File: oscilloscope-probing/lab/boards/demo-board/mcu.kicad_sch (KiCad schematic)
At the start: 75 parts, among them J4 CORTEX_DEBUG_ETM, J6 CONN_01X06, SW3 SWITCH, SW4 SWITCH, SW5 SWITCH, SW6 SWITCH, SW7 SWITCH, U4 XC7A35T-2FGG484I, U5 STM32H750XBH6, U6 ECS-1612MV-250-CN, U7 ECS-1612MV-250-CN, U8 S25FL064LABMFI013

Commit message: Continued routing demo board
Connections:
- net DPAD_N: now also U5.N15 (PJ6); no longer U5.E10 (PJ13)
- net DPAD_S: now also U5.L14 (PJ10); no longer U5.D11 (PJ12)
- net DPAD_SEL: now also U5.M14 (PJ9); no longer U5.D10 (PJ14)
- net DPAD_W: now also U5.N14 (PJ7); no longer U5.L14 (PJ10)
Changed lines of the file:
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@@
 	)
 	(no_connect
-		(at 107.95 232.41)
-	)
-	(no_connect
 		(at 35.56 140.97)
 	)
@@
 	)
 	(no_connect
+		(at 107.95 247.65)
+	)
+	(no_connect
 		(at 107.95 222.25)
 	)
@@
 	)
 	(no_connect
+		(at 107.95 250.19)
+	)
+	(no_connect
 		(at 107.95 148.59)
 	)
@@
 	)
 	(no_connect
-		(at 107.95 240.03)
-	)
-	(no_connect
 		(at 35.56 101.6)
 	)
@@
 	)
 	(no_connect
-		(at 107.95 234.95)
+		(at 107.95 57.15)
 	)
 	(no_connect
-		(at 107.95 57.15)
+		(at 107.95 252.73)
 	)
 	(no_connect
@@
 	)
 	(label "DPAD_S"
-		(at 107.95 247.65 180)
+		(at 107.95 242.57 180)
 		(effects
 			(font
@@
 	)
 	(label "DPAD_W"
-		(at 107.95 242.57 180)
+		(at 107.95 234.95 180)
 		(effects
 			(font
@@
 	)
 	(label "DPAD_SEL"
-		(at 107.95 252.73 180)
+		(at 107.95 240.03 180)
 		(effects
 			(font
@@
 	)
 	(label "DPAD_N"
-		(at 107.95 250.19 180)
+		(at 107.95 232.41 180)
 		(effects
 			(font

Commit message: Continued demo board layout
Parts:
- removed J6: CONN_01X06, azonenberg_pcb:CONN_HEADER_2.54MM_1x6_REFLOW, symbol conn:CONN_01X06
- added J24: PMOD_HOST, azonenberg_pcb:CONN_HEADER_2.54MM_2x6_RA_PMOD_HOST, symbol special-azonenberg:PMOD_HOST
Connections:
- net 3V3: now also J24.12 (3V3), J24.6 (3V3)
- net DPY_BS: now also U5.A16 (PI0); no longer U5.H4 (PF3)
- net DPY_BUSY_N: now also U5.B16 (PH15); no longer U5.J5 (PF4)
- net DPY_DC: now also U5.B15 (PI2); no longer U5.J4 (PF5)
- net DPY_RST_N: now also U5.A15 (PI1); no longer U5.K4 (PF8)
- net FMC_A19: now also U4.N15 (IO_25_14); no longer U4.V20 (IO_L11N_T1_SRCC_14)
- net FMC_A20: now also U4.N14 (IO_L23N_T3_A02_D18_14); no longer U4.R18 (IO_L20P_T3_A08_D24_14)
- net FMC_A21: now also U4.N13 (IO_L23P_T3_A03_D19_14); no longer U4.T21 (IO_L4P_T0_D04_14)
- net FMC_A22: now also U4.U20 (IO_L11P_T1_SRCC_14); no longer U4.P15 (IO_L22P_T3_A05_D21_14)
- net FMC_AD2: now also U4.T18 (IO_L20N_T3_A07_D23_14); no longer U4.U18 (IO_L18N_T2_A11_D27_14)
- net FMC_AD8: now also U4.P15 (IO_L22P_T3_A05_D21_14); no longer U4.T18 (IO_L20N_T3_A07_D23_14)
- net FMC_NBL0: now also U4.U18 (IO_L18N_T2_A11_D27_14); no longer U4.N13 (IO_L23P_T3_A03_D19_14)
- net FMC_NBL1: now also U4.V17 (IO_L16P_T2_CSI_B_14); no longer U4.N14 (IO_L23N_T3_A02_D18_14)
- net FMC_NE1: now also U4.R14 (IO_L19N_T3_A09_D25_VREF_14); no longer U4.V17 (IO_L16P_T2_CSI_B_14)
- net FMC_NE2: now also U4.T21 (IO_L4P_T0_D04_14); no longer U4.U20 (IO_L11P_T1_SRCC_14)
- net FMC_NE3: now also U4.R18 (IO_L20P_T3_A08_D24_14); no longer U4.N15 (IO_25_14)
- net FMC_NL_NADV: now also U4.V20 (IO_L11N_T1_SRCC_14); no longer U4.R14 (IO_L19N_T3_A09_D25_VREF_14)
- net GND: now also J24.11 (GND), J24.5 (GND)
- net MCU_TRIG: now also U5.E4 (PI8); no longer U5.A16 (PI0)
- net MCU_PMOD_DQ4: now reaches U5.R3 (PA6)
- net MCU_PMOD_DQ4: now also J24.7 (D4)
- net MCU_PMOD_DQ2: now reaches U5.U2 (PA3)
- net MCU_PMOD_DQ2: now also J24.3 (D2)
- net MCU_PMOD_DQ5: now reaches U5.N2 (PH2)
- net MCU_PMOD_DQ5: now also J24.8 (D5)
- net MCU_PMOD_DQ6: now reaches U5.P2 (PH3)
- net MCU_PMOD_DQ6: now also J24.9 (D6)
- net MCU_PMOD_DQ7: now reaches U5.P3 (PH4)
- net MCU_PMOD_DQ7: now also J24.10 (D7)
- net MCU_PMOD_DQ3: now reaches U5.T4 (PC4)
- net MCU_PMOD_DQ3: now also J24.4 (D3)
- net MCU_PMOD_DQ0: now reaches U5.U4 (PC5)
- net MCU_PMOD_DQ0: now also J24.1 (D0)
- net MCU_PMOD_DQ1: now reaches U5.T5 (PB1)
- net MCU_PMOD_DQ1: now also J24.2 (D1)
- net FPGA_UART_CTS_N: no longer names the net of U4.V19 (IO_L14N_T2_SRCC_14)
- net FPGA_UART_RTS_N: no longer names the net of U4.AA19 (IO_L15P_T2_DQS_RDWR_B_14)
- net FPGA_UART_RX: no longer names the net of U4.R19 (IO_L5N_T0_D07_14)
- net FPGA_UART_TX: no longer names the net of U4.P19 (IO_L5P_T0_D06_14)
- no-connect marks 115 -> 110
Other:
- note removed: "FTDI cable pinout"
- moved on the sheet: TP12

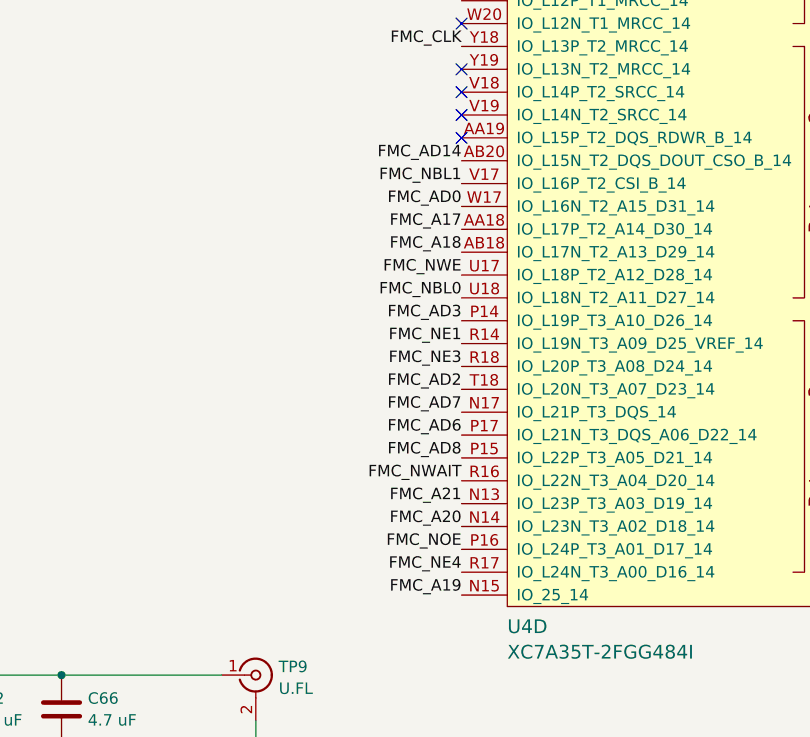
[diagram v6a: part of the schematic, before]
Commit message: Under 100 unrouted
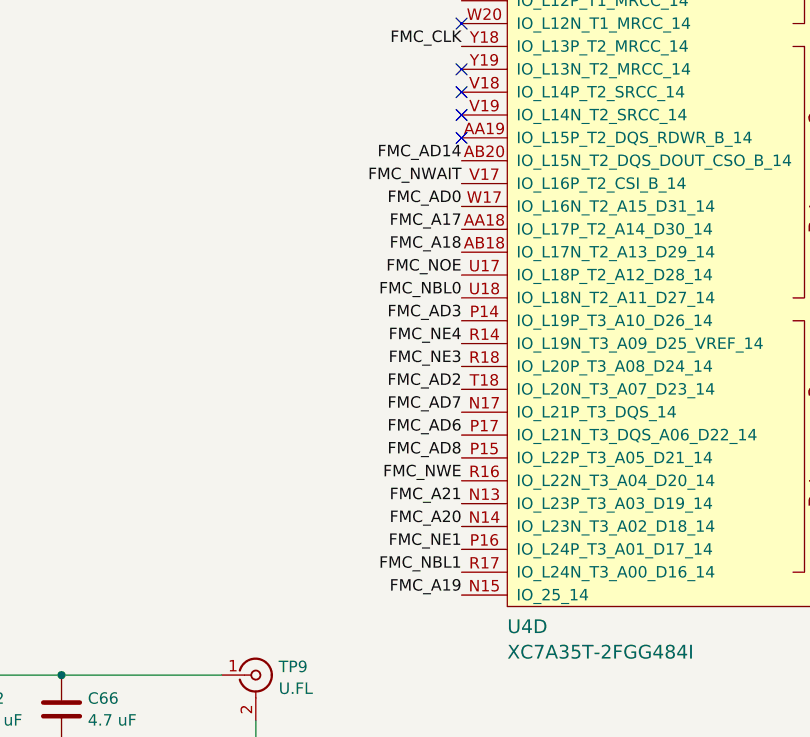
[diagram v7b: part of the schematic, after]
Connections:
- net FMC_NBL1: now also U4.R17 (IO_L24N_T3_A00_D16_14); no longer U4.V17 (IO_L16P_T2_CSI_B_14)
- net FMC_NE1: now also U4.P16 (IO_L24P_T3_A01_D17_14); no longer U4.R14 (IO_L19N_T3_A09_D25_VREF_14)
- net FMC_NE4: now also U4.R14 (IO_L19N_T3_A09_D25_VREF_14); no longer U4.R17 (IO_L24N_T3_A00_D16_14)
- net FMC_NOE: now also U4.U17 (IO_L18P_T2_A12_D28_14); no longer U4.P16 (IO_L24P_T3_A01_D17_14)
- net FMC_NWAIT: now also U4.V17 (IO_L16P_T2_CSI_B_14); no longer U4.R16 (IO_L22N_T3_A04_D20_14)
- net FMC_NWE: now also U4.R16 (IO_L22N_T3_A04_D20_14); no longer U4.U17 (IO_L18P_T2_A12_D28_14)
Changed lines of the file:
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@@
 	)
 	(label "FMC_NWE"
-		(at 347.98 115.57 180)
+		(at 347.98 138.43 180)
 		(effects
 			(font
@@
 	)
 	(label "FMC_NE1"
-		(at 347.98 123.19 180)
+		(at 347.98 146.05 180)
 		(effects
 			(font
@@
 	)
 	(label "FMC_NE4"
-		(at 347.98 148.59 180)
+		(at 347.98 123.19 180)
 		(effects
 			(font
@@
 	)
 	(label "FMC_NWAIT"
-		(at 347.98 138.43 180)
+		(at 347.98 105.41 180)
 		(effects
 			(font
@@
 	)
 	(label "FMC_NBL1"
-		(at 347.98 105.41 180)
+		(at 347.98 148.59 180)
 		(effects
 			(font
@@
 	)
 	(label "FMC_NOE"
-		(at 347.98 146.05 180)
-		(effects
-			(font
+		(at 347.98 115.57 180)
+		(effects
+			(font

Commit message: Continued layout, 55 unrouted
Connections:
- net MCU_DONE: now also U5.B17 (PH14); no longer U5.G4 (PF0)
- net MCU_TRIG: now also U5.C1 (PC15); no longer U5.E4 (PI8)
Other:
- moved on the sheet: TP12
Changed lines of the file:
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@@
 	)
 	(no_connect
+		(at 107.95 190.5)
+	)
+	(no_connect
 		(at 35.56 148.59)
 	)
@@
 	)
 	(no_connect
+		(at 107.95 24.13)
+	)
+	(no_connect
 		(at 107.95 140.97)
 	)
@@
 	)
 	(no_connect
-		(at 107.95 153.67)
-	)
-	(no_connect
 		(at 35.56 99.06)
 	)
@@
 	)
 	(no_connect
-		(at 35.56 161.29)
-	)
-	(no_connect
 		(at 107.95 59.69)
 	)
@@
 	(wire
 		(pts
+			(xy 24.13 161.29) (xy 35.56 161.29)
+		)
+		(stroke
+			(width 0)
+			(type default)
+		)
+	)
+	(wire
+		(pts
 			(xy 185.42 125.73) (xy 185.42 135.89)
 		)
@@
 	(wire
 		(pts
-			(xy 88.9 190.5) (xy 107.95 190.5)
-		)
-		(stroke
-			(width 0)
-			(type default)
-		)
-	)
-	(wire
-		(pts
 			(xy 270.51 106.68) (xy 270.51 109.22)
 		)
@@
 	)
 	(label "MCU_TRIG"
-		(at 88.9 190.5 0)
+		(at 24.13 161.29 0)
 		(effects
 			(font
@@
 	(hierarchical_label "MCU_DONE"
 		(shape output)
-		(at 107.95 24.13 180)
+		(at 107.95 153.67 180)
 		(effects
 			(font
@@
 	(symbol
 		(lib_id "conn:CONN_01X01")
-		(at 83.82 190.5 0)
+		(at 19.05 161.29 0)
 		(mirror y)
 		(unit 1)
@@
 		(dnp no)
 		(property "Reference" "TP12"
-			(at 81.915 189.2878 0)
+			(at 21.59 163.83 0)
 			(effects
 				(font
@@
 		)
 		(property "Value" "TESTCLIP"
-			(at 81.915 191.7121 0)
+			(at 21.59 166.2543 0)
 			(effects
 				(font
@@
 		)
 		(property "Footprint" "azonenberg_pcb:TESTPOINT_SMT_KEYSTONE_5016"
-			(at 83.82 190.5 0)
+			(at 19.05 161.29 0)
 			(effects
 				(font
@@
 		)
 		(property "Datasheet" ""
-			(at 83.82 190.5 0)
+			(at 19.05 161.29 0)
 			(effects
 				(font
@@
 		)
 		(property "Description" "Connector, single row, 01x01, pin header"
-			(at 83.82 190.5 0)
+			(at 19.05 161.29 0)
 			(effects
 				(font
